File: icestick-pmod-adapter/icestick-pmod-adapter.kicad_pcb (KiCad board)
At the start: 2 copper layers, 45.7 x 40.6 mm, 3 parts, among them J1 Conn_02x06_Odd_Even, J2 Conn_02x06_Odd_Even, U1 icestick

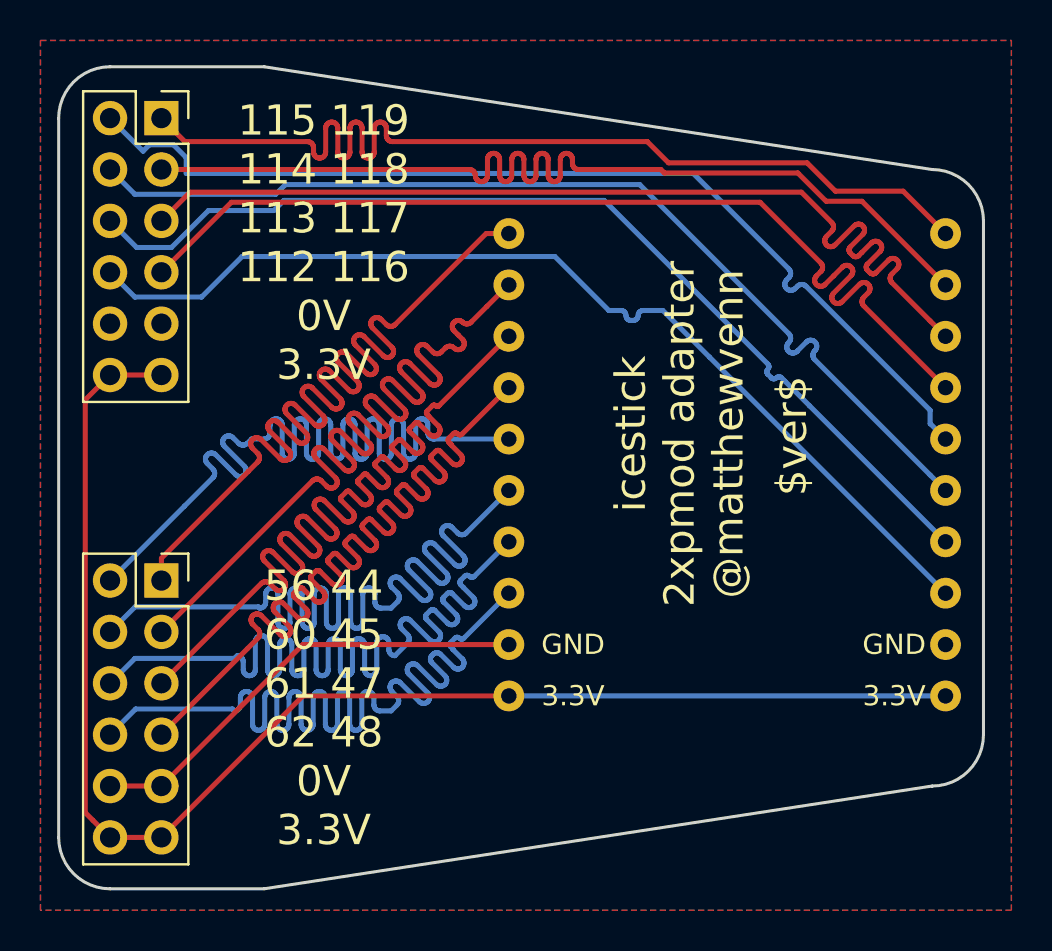
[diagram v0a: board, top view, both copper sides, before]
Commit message: added bitlink
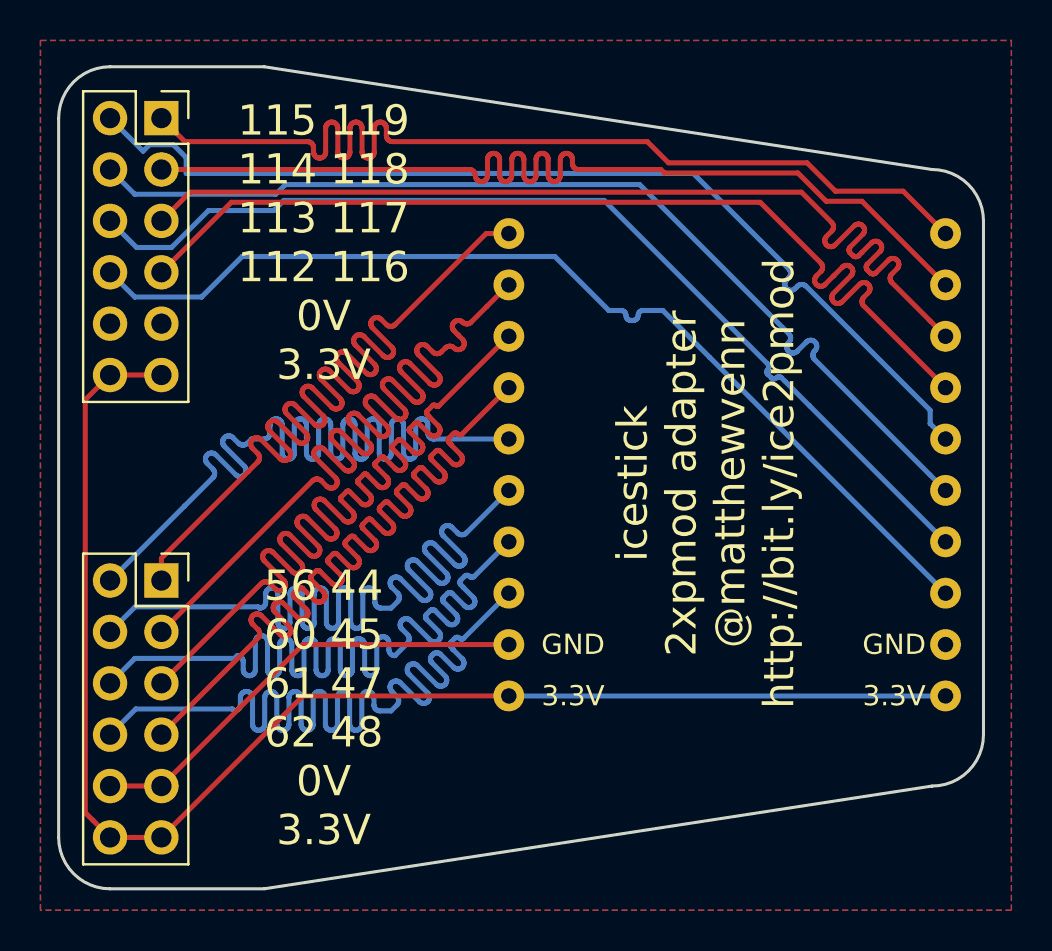
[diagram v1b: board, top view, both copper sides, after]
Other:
- board text added: "icestick 2xpmod adapter @matthewvenn http://bit.ly/ice2pmod"
- board text removed: "icestick 2xpmod adapter @matthewvenn"
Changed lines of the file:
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@@
     (effects (font (size 1.5 1.5) (thickness 0.3)))
   )
-  (gr_text $ver$ (at 125.15 132.55 90) (layer F.SilkS)
+  (gr_text $ver$ (at 122.35 133.7 90) (layer B.SilkS)
+    (effects (font (size 1.5 1.5) (thickness 0.3)) (justify mirror))
+  )
+  (gr_text "icestick\n2xpmod adapter\n@matthewvenn\nhttp://bit.ly/ice2pmod" (at 120.9 134.9 90) (layer F.SilkS)
     (effects (font (size 1.5 1.5) (thickness 0.3)))
   )
-  (gr_text "icestick\n2xpmod adapter\n@matthewvenn\n" (at 119.6 132.45 90) (layer F.SilkS)
-    (effects (font (size 1.5 1.5) (thickness 0.3)))
-  )
